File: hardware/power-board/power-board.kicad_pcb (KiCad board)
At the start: 2 copper layers, 188 x 64.5 mm, 18 parts, among them J1 SW_SPST, J2 Conn_01x04, K1 SPST-NO, K2 SPST-NO, P1 IEC320-C14, P2 IEC320-C13, P3 IEC320-C13, U1 NUD3112DMT1G

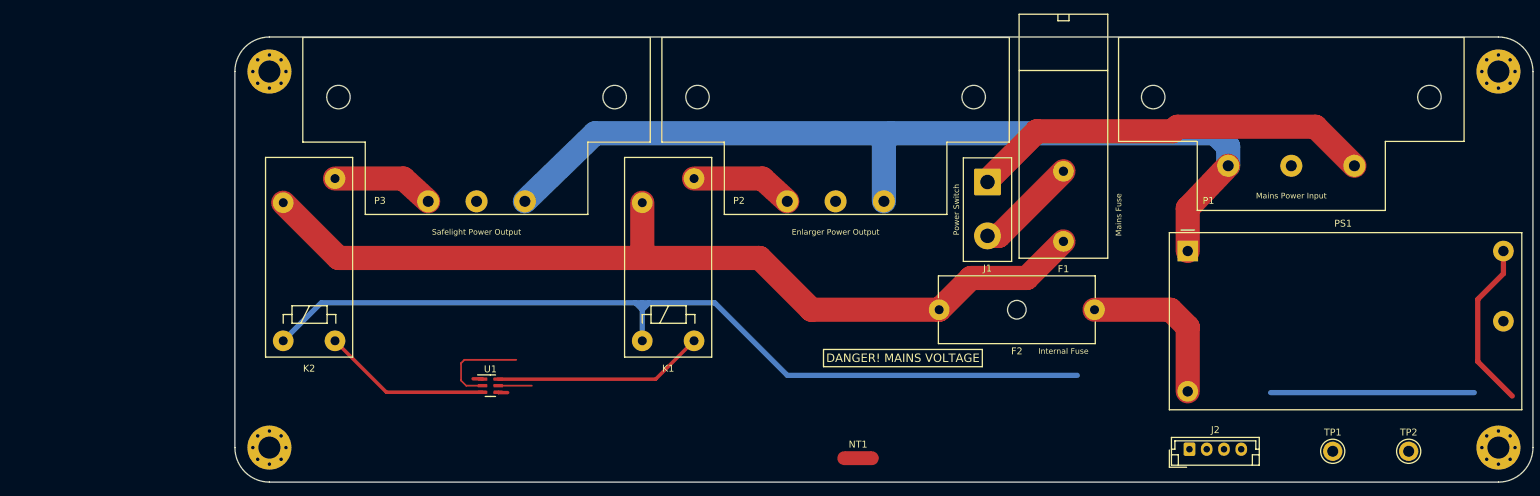
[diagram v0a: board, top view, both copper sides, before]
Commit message: WIP of adding XLR5 jack and making mechanical adjustments
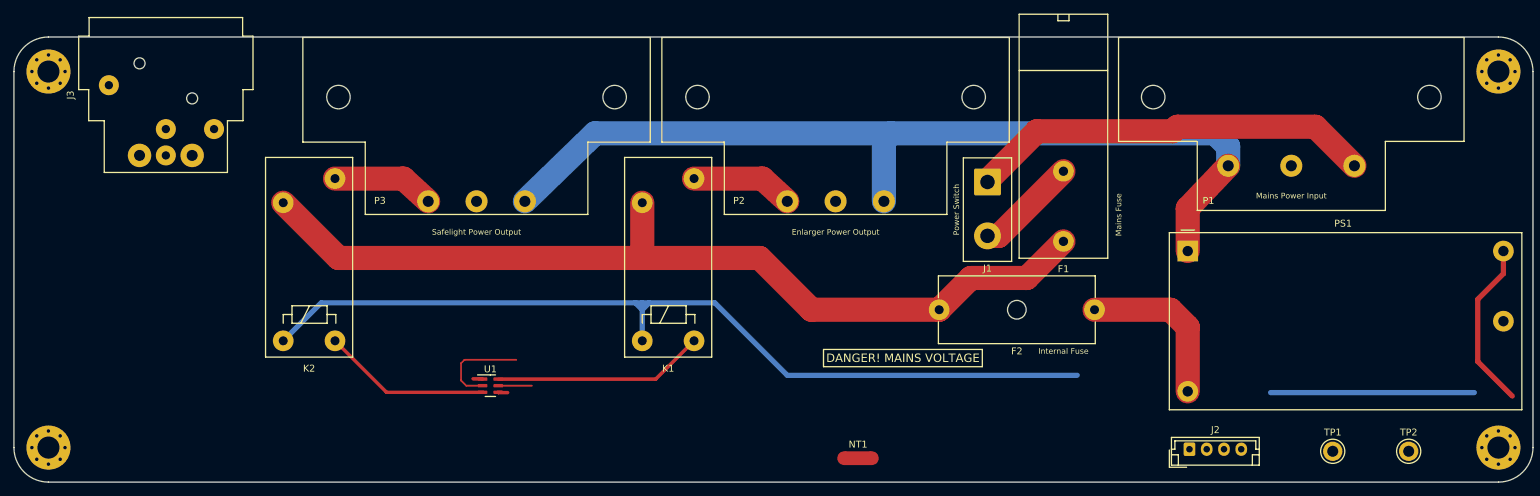
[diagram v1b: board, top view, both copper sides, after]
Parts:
- added J3: DMX512 Out Jack, Connector_Audio:Jack_XLR_Neutrik_NC5FBH_Horizontal, F.Cu at (2.19, 37.1)
- moved H1 32.0 mm to (-11.0, 25.0)
- moved H4 32.0 mm to (-11.0, 79.5)
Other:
- board size 188 x 64.5 mm -> 220 x 64.5 mm
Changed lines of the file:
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@@
   (net 13 "/RELAY_SAFELIGHT")
   (net 14 "Earth")
+  (net 15 "unconnected-(J3-Pad1)")
+  (net 16 "unconnected-(J3-Pad2)")
+  (net 17 "unconnected-(J3-Pad3)")
+  (net 18 "unconnected-(J3-Pad4)")
+  (net 19 "unconnected-(J3-Pad5)")
   (footprint "Fuse:Fuseholder_Cylinder-5x20mm_Schurter_0031_8201_Horizontal_Open" (layer "F.Cu")
     (at 140.5 59.5 180)
@@
   )
   (footprint "MountingHole:MountingHole_3.2mm_M3_Pad_Via" (layer "F.Cu")
-    (at 21 25)
+    (at -11 25)
     (descr "Mounting Hole 3.2mm, M3")
     (tags "mounting hole 3.2mm m3")
@@
   )
   (footprint "MountingHole:MountingHole_3.2mm_M3_Pad_Via" (layer "F.Cu")
-    (at 21 79.464466)
+    (at -11 79.464466)
     (descr "Mounting Hole 3.2mm, M3")
     (tags "mounting hole 3.2mm m3")
@@
       (net 1 "GND") (pinfunction "2") (pintype "passive"))
   )
+  (footprint "Connector_Audio:Jack_XLR_Neutrik_NC5FBH_Horizontal" (layer "F.Cu")
+    (at 2.19 37.15 90)
+    (descr "B Series, 5 pole female XLR receptacle, grounding: separate ground contact to mating connector shell and front panel, horizontal PCB mount, https://www.neutrik.com/en/product/nc5fbh")
+    (tags "neutrik xlr b")
+    (property "Description" "XLR Connectors 5C PCB FEMALE RECEPT")
+    (property "Manufacturer" "Neutrik")
+    (property "Manufacturer PN" "NC5FBH")
+    (property "Sheetfile" "power-board.kicad_sch")
+    (property "Sheetname" "")
+    (property "Supplier" "Mouser")
+    (property "Supplier PN" "568-NC5FBH")
+    (attr through_hole)
+    (fp_text reference "J3" (at 8.75 -10 90) (layer "F.SilkS")
+      (effects (font (size 1 1) (thickness 0.15)))
+    )
+    (fp_text value "DMX512 Out Jack" (at 8.75 17.5 90) (layer "F.Fab")
+      (effects (font (size 1 1) (thickness 0.15)))
+    )
+    (fp_text user "${REFERENCE}" (at 14.8 3.81 90) (layer "F.Fab")
+      (effects (font (size 1 1) (thickness 0.15)))
+    )
+    (fp_line (start 17.27 -7.31) (end 19.97 -7.31) (layer "F.SilkS") (width 0.12))
+    (fp_line (start 17.27 -8.81) (end 17.27 -7.31) (layer "F.SilkS") (width 0.12))
+    (fp_line (start 9.53 -7.36) (end 9.53 -8.81) (layer "F.SilkS") (width 0.12))
+    (fp_line (start 9.53 14.98) (end 5.03 14.98) (layer "F.SilkS") (width 0.12))
+    (fp_line (start 17.27 -8.81) (end 9.53 -8.81) (layer "F.SilkS") (width 0.12))
+    (fp_line (start 5.03 12.73) (end 5.03 14.98) (layer "F.SilkS") (width 0.12))
+    (fp_line (start 19.97 -7.31) (end 19.97 14.93) (layer "F.SilkS") (width 0.12))
+    (fp_line (start 5.03 12.73) (end -2.47 12.73) (layer "F.SilkS") (width 0.12))
+    (fp_line (start 9.53 16.43) (end 9.53 14.98) (layer "F.SilkS") (width 0.12))
+    (fp_line (start 17.27 14.93) (end 19.97 14.93) (layer "F.SilkS") (width 0.12))
+    (fp_line (start 17.27 16.43) (end 9.53 16.43) (layer "F.SilkS") (width 0.12))
+    (fp_line (start -2.47 -5.11) (end -2.47 12.73) (layer "F.SilkS") (width 0.12))
+    (fp_line (start 5.03 -5.11) (end -2.47 -5.11) (layer "F.SilkS") (width 0.12))
+    (fp_line (start 9.53 -7.36) (end 5.03 -7.36) (layer "F.SilkS") (width 0.12))
+    (fp_line (start 5.03 -5.11) (end 5.03 -7.36) (layer "F.SilkS") (width 0.12))
+    (fp_line (start 17.27 14.93) (end 17.27 16.43) (layer "F.SilkS") (width 0.12))
+    (fp_line (start 17.15 -8.69) (end 17.15 16.31) (layer "Dwgs.User") (width 0.1))
+    (fp_line (start 20.35 -9.19) (end -2.85 -9.19) (layer "F.CrtYd") (width 0.05))
+    (fp_line (start 20.35 16.81) (end -2.85 16.81) (layer "F.CrtYd") (width 0.05))
+    (fp_line (start 20.35 -9.19) (end 20.35 16.81) (layer "F.CrtYd") (width 0.05))
+    (fp_line (start -2.85 -9.19) (end -2.85 16.81) (layer "F.CrtYd") (width 0.05))
+    (fp_line (start 9.65 16.31) (end 9.65 -8.69) (layer "F.Fab") (width 0.1))
+    (fp_line (start -2.35 -4.99) (end -2.35 12.61) (layer "F.Fab") (width 0.1))
+    (fp_line (start 17.15 -7.19) (end 19.85 -7.19) (layer "F.Fab") (width 0.1))
+    (fp_line (start 17.15 16.31) (end 9.65 16.31) (layer "F.Fab") (width 0.1))
+    (fp_line (start 5.15 14.86) (end 5.15 -7.24) (layer "F.Fab") (width 0.1))
+    (fp_line (start 19.85 -7.19) (end 19.85 14.81) (layer "F.Fab") (width 0.1))
+    (fp_line (start 5.15 14.86) (end 9.65 14.86) (layer "F.Fab") (width 0.1))
+    (fp_line (start 5.15 -4.99) (end -2.35 -4.99) (layer "F.Fab") (width 0.1))
+    (fp_line (start 5.15 12.61) (end -2.35 12.61) (layer "F.Fab") (width 0.1))
+    (fp_line (start 19.85 14.81) (end 17.15 14.81) (layer "F.Fab") (width 0.1))
+    (fp_line (start 9.65 -7.24) (end 5.15 -7.24) (layer "F.Fab") (width 0.1))
+    (fp_line (start 9.65 -8.69) (end 17.15 -8.69) (layer "F.Fab") (width 0.1))
+    (fp_line (start 17.15 -8.69) (end 17.15 16.31) (layer "F.Fab") (width 0.1))
+    (pad "" np_thru_hole circle (at 13.34 0 90) (size 1.6 1.6) (drill 1.6) (layers *.Cu *.Mask))
+    (pad "" np_thru_hole circle (at 8.26 7.62 90) (size 1.6 1.6) (drill 1.6) (layers *.Cu *.Mask))
+    (pad "1" thru_hole circle (at 0 0 90) (size 3.4 3.4) (drill 1.6) (layers *.Cu *.Mask)
+      (net 15 "unconnected-(J3-Pad1)") (pinfunction "P1") (pintype "passive+no_connect"))
+    (pad "2" thru_hole circle (at 3.815 3.81 90) (size 2.9 2.9) (drill 1.2) (layers *.Cu *.Mask)
+      (net 16 "unconnected-(J3-Pad2)") (pinfunction "P2") (pintype "passive+no_connect"))
+    (pad "3" thru_hole circle (at 0 3.81 90) (size 2.9 2.9) (drill 1.2) (layers *.Cu *.Mask)
+      (net 17 "unconnected-(J3-Pad3)") (pinfunction "P3") (pintype "passive+no_connect"))
+    (pad "4" thru_hole circle (at 3.815 10.79 90) (size 2.9 2.9) (drill 1.2) (layers *.Cu *.Mask)
+      (net 18 "unconnected-(J3-Pad4)") (pinfunction "P3") (pintype "passive+no_connect"))
+    (pad "5" thru_hole circle (at 0 7.62 90) (size 3.4 3.4) (drill 1.6) (layers *.Cu *.Mask)
+      (net 19 "unconnected-(J3-Pad5)") (pinfunction "P5") (pintype "passive+no_connect"))
+    (pad "G" thru_hole circle (at 10.17 -4.44 90) (size 2.9 2.9) (drill 1.2) (layers *.Cu *.Mask)
+      (net 14 "Earth") (pintype "passive"))
+    (model "${KIPRJMOD}/../library/3dmodels/lib_fp.3dshapes/Neutrik_NC5FBH.step"
+      (offset (xyz 17.5 -3.81 12.5))
+      (scale (xyz 1 1 1))
+      (rotate (xyz -90 0 90))
+    )
+  )
   (footprint "TestPoint:TestPoint_Keystone_5005-5009_Compact" (layer "F.Cu")
     (at 175 80)
@@
   (gr_line (start 121.5 37.5) (end 128.5 37.5) (layer "F.SilkS") (width 0.1524))
   (gr_arc (start 204 79.464466) (mid 202.535534 83) (end 199 84.464466) (layer "Edge.Cuts") (width 0.0381))
-  (gr_line (start 21 84.464466) (end 199 84.464466) (layer "Edge.Cuts") (width 0.0381))
-  (gr_arc (start 21 84.464466) (mid 17.464466 83) (end 16 79.464466) (layer "Edge.Cuts") (width 0.0381))
-  (gr_line (start 21 20) (end 199 20) (layer "Edge.Cuts") (width 0.0381))
-  (gr_arc (start 16 25) (mid 17.464466 21.464466) (end 21 20) (layer "Edge.Cuts") (width 0.0381))
+  (gr_line (start -11 84.464466) (end 199 84.464466) (layer "Edge.Cuts") (width 0.0381))
+  (gr_arc (start -11 84.464466) (mid -14.535532 83) (end -16 79.464466) (layer "Edge.Cuts") (width 0.0381))
+  (gr_line (start -11 20) (end 199 20) (layer "Edge.Cuts") (width 0.0381))
+  (gr_arc (start -16 25) (mid -14.535534 21.464466) (end -11 20) (layer "Edge.Cuts") (width 0.0381))
   (gr_line (start 204 25) (end 204 79.464466) (layer "Edge.Cuts") (width 0.0381))
-  (gr_line (start 16 25) (end 16 79.464466) (layer "Edge.Cuts") (width 0.0381))
+  (gr_line (start -16 25) (end -16 79.464466) (layer "Edge.Cuts") (width 0.0381))
   (gr_arc (start 199 20) (mid 202.535534 21.464466) (end 204 25) (layer "Edge.Cuts") (width 0.0381))
   (gr_text "DANGER! MAINS VOLTAGE" (at 106 49.75 180) (layer "B.SilkS")

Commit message: Resized board outline to tightly fit XLR5 connector
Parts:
- removed H3, H4: MountingHole_Pad, MountingHole:MountingHole_3.2mm_M3_Pad_Via
- moved H1 90.7 mm to (40.0, 100.0)
- moved H2 80.1 mm to (227.0, 100.0)
- moved K2 47.7 mm to (60.0, 94.1)
- moved J3 47.4 mm to (45.2, 57.1)
- moved F2 42.1 mm to (177.5, 79.5)
- moved J1 42.1 mm to (162.0, 61.0)
- moved K1 42.1 mm to (112.0, 84.0)
- moved NT1 42.1 mm to (143.2, 101.0)
- moved P1 42.1 mm to (206.0, 48.7)
- moved P2 42.1 mm to (140.0, 48.7)
- moved P3 42.1 mm to (88.0, 48.7)
- moved U1 42.1 mm to (90.0, 90.5)
- moved F1 42.1 mm to (173.0, 69.6)
- moved PS1 35.3 mm to (183.1, 70.9)
- moved J2 26.9 mm to (172.2, 99.7)
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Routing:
- net +12V: track 184.1 -> 76.7 mm
- net Net-(F2-Pad1): track 23.9 -> 0.00 mm
- net NEUT: track 134.4 -> 119.7 mm
- net LINE: track 131.9 -> 134.4 mm
- net Net-(K2-Pad1): track 24.4 -> 22.5 mm
- net Net-(K2-Pad3): track 14.8 -> 16.3 mm
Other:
- board size 220 x 64.5 mm -> 197 x 65 mm

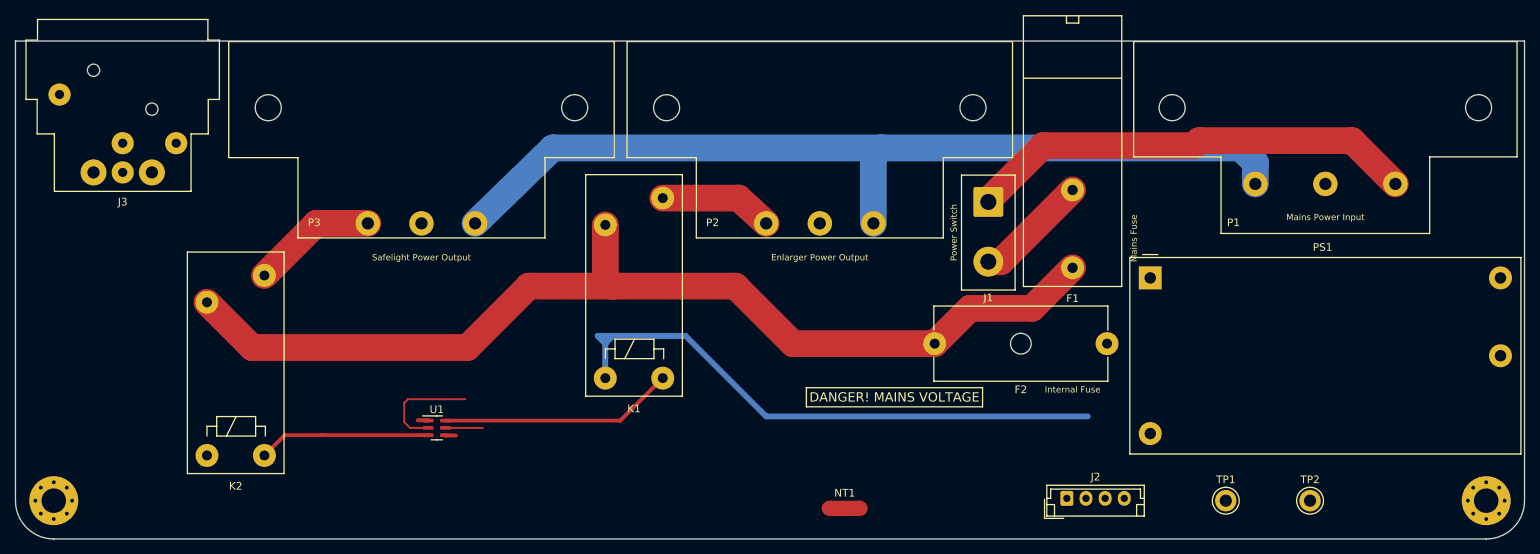
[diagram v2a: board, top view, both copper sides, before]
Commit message: Initial addition of RS-485 interface components for DMX512
So far this is just getting the line driver on the board, in addition to
a few support components. Passives and internal connectors are still
placeholders.

The DMX512 spec says the transmitter should be earth referenced, not
isolated, so that helps make our driver and connector decisions.
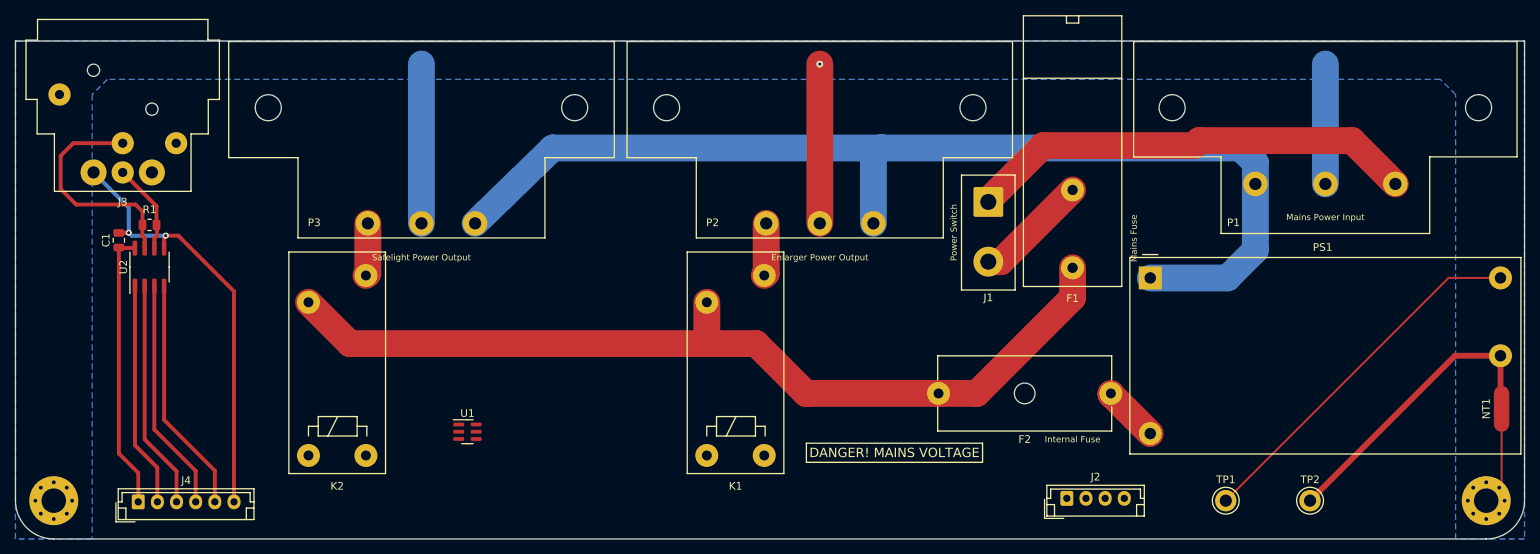
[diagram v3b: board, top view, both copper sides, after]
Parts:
- added C1: 0.1uF, Capacitor_SMD:C_0805_2012Metric, F.Cu at (48.5, 66.0)
- added J4: DMX512, Connector_JST:JST_EH_B6B-EH-A_1x06_P2.50mm_Vertical, F.Cu at (51.0, 100.2)
- added R1: 120R, Resistor_SMD:R_0805_2012Metric, F.Cu at (52.5, 64.0)
- added U2: MAX3075E, Package_SO:SOIC-8_3.9x4.9mm_P1.27mm, F.Cu at (52.5, 69.5)
- moved NT1 86.7 mm to (229.0, 88.0), turned to 90 degrees
- moved K1 16.7 mm to (125.2, 94.1)
- moved K2 13.2 mm to (73.2, 94.1)
- moved F2 6.52 mm to (178.0, 86.0)
- moved U1 4.03 mm to (94.0, 91.0)
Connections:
- H1 pad 1: GND -> Earth
- H2 pad 1: GND -> Earth
- J3 pad 1: unconnected-(J3-Pad1) -> GND
- J3 pad 2: unconnected-(J3-Pad2) -> /RS-485-
- J3 pad 3: unconnected-(J3-Pad3) -> /RS-485+
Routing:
- net GND: track 2.77 -> 94.8 mm, vias 0 -> 2
- net Earth: track 0.00 -> 68.1 mm, vias 0 -> 1
- net +3.3V: track 0.00 -> 36.4 mm
- net /TX: track 0.00 -> 30.9 mm
- net Net-(K1-Pad1): track 30.7 -> 0.00 mm
- net /TX_EN: track 0.00 -> 30.4 mm
- net /RS-485-: track 0.00 -> 29.9 mm
- net /RX_EN: track 0.00 -> 29.9 mm
- net /RX: track 0.00 -> 29.4 mm
- net +12V: track 76.7 -> 47.9 mm
- net NEUT: track 119.7 -> 143.6 mm
- net Net-(K2-Pad1): track 22.5 -> 0.00 mm
- net LINE: track 134.4 -> 119.5 mm
- net /RELAY_ENLARGER: track 14.1 -> 0.00 mm
- net /RS-485+: track 0.00 -> 11.9 mm
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- added copper zone on B.Cu, net Earth

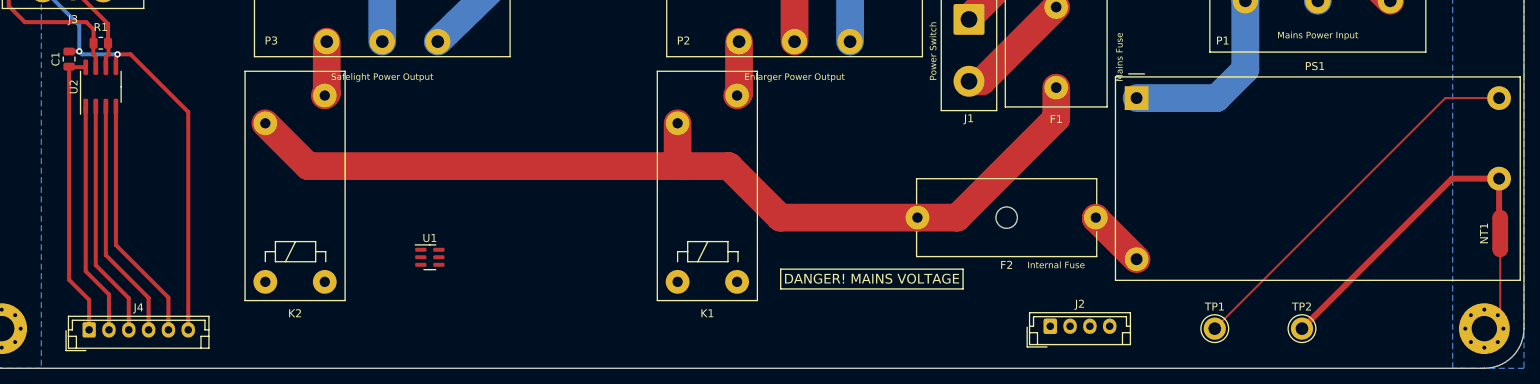
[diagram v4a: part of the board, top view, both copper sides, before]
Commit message: Updated components now in place
Everything still needs to be rearranged and rerouted.
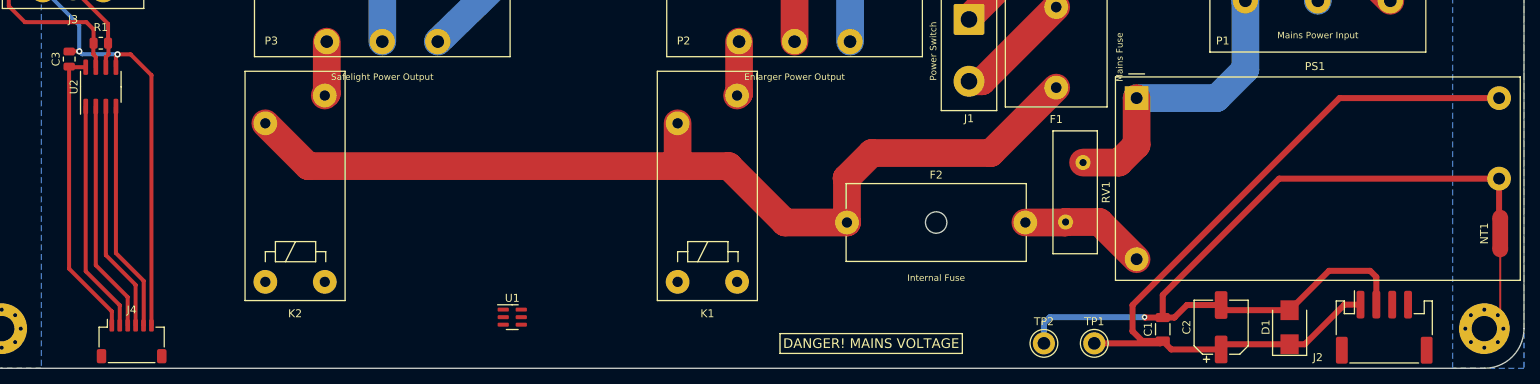
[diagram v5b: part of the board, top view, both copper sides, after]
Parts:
- added C2: 10uF, Capacitor_SMD:CP_Elec_6.3x5.4, F.Cu at (193.8, 99.8)
- added C3: 0.1uF, Capacitor_SMD:C_0805_2012Metric, F.Cu at (48.5, 66.0)
- added D1: SMBJ20A, Diode_SMD:D_SMB, F.Cu at (202.4, 99.8)
- added RV1: S14K350, lib_fp:RV_Disc_D15.5mm_W5.6mm_P7.5mm, F.Cu at (174.2, 86.6)
- C1: footprint Capacitor_SMD:C_0805_2012Metric -> Capacitor_SMD:C_1206_3216Metric
- J2: value Conn_01x04 -> Main Board; footprint Connector_JST:JST_EH_B4B-EH-A_1x04_P2.50mm_Vertical -> Connector_JST:JST_PH_S4B-PH-SM4-TB_1x04-1MP_P2.00mm_Horizontal
- J4: footprint Connector_JST:JST_EH_B6B-EH-A_1x06_P2.50mm_Vertical -> Connector_JST:JST_SH_SM06B-SRSS-TB_1x06-1MP_P1.00mm_Horizontal
- moved C1 142.1 mm to (186.4, 100.1)
- moved J2 42.1 mm to (214.4, 99.8)
- moved TP2 32.6 mm to (171.4, 101.9)
- moved F2 31.4 mm to (146.6, 86.6), turned to 0 degrees
- moved TP1 15.3 mm to (177.8, 101.9)
- moved U1 12.8 mm to (104.4, 98.6)
- moved J4 5.55 mm to (56.4, 101.6)
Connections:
- C1 pad 1: +3.3V -> +12V
- F2 pad 1: Net-(F2-Pad1) -> LINE
- F2 pad 2: LINE -> Net-(F2-Pad2)
- J2 pad 2: /RELAY_ENLARGER -> GND
- J2 pad 3: /RELAY_SAFELIGHT -> /RELAY_ENLARGER
- J2 pad 4: GND -> /RELAY_SAFELIGHT
- PS1 pad 2: Net-(F2-Pad1) -> Net-(F2-Pad2)
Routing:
- net GND: track 94.8 -> 162.6 mm, vias 2 -> 3
- net +12V: track 47.9 -> 101.2 mm
- net Net-(F2-Pad2): track 0.00 -> 16.0 mm
- net NEUT: track 143.6 -> 157.2 mm
- net Net-(F2-Pad1): track 7.37 -> 0.00 mm
- net /TX: track 30.9 -> 29.1 mm
- net LINE: track 119.5 -> 121.1 mm
- net /TX_EN: track 30.4 -> 29.2 mm
- net +3.3V: track 36.4 -> 37.0 mm
- net /RX_EN: track 29.9 -> 29.3 mm
